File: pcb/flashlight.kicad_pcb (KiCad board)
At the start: 2 copper layers, 16.8 x 15.8 mm, 25 parts, among them IC1 TPS61200, IC2 PIC10F320

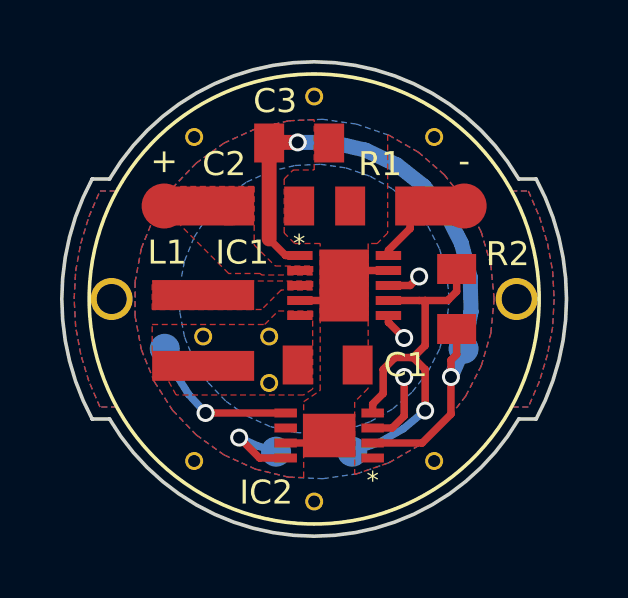
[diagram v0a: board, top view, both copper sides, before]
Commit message: increase width of the vdd and led traces
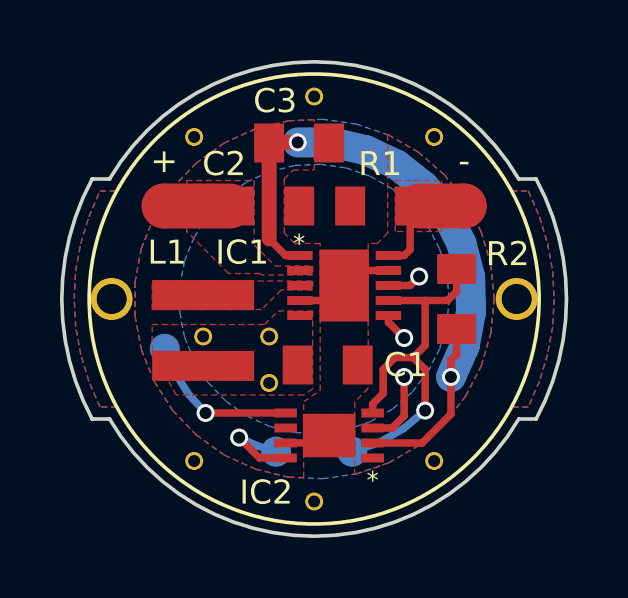
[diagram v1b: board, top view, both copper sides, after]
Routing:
- added copper zone on F.Cu, net N$5
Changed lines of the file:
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@@
   (layers
     (0 F.Cu signal)
-    (31 B.Cu signal)
+    (31 B.Cu signal hide)
     (32 B.Adhes user)
     (33 F.Adhes user)
@@
     (36 B.SilkS user)
     (37 F.SilkS user)
-    (38 B.Mask user)
+    (38 B.Mask user hide)
     (39 F.Mask user)
     (40 Dwgs.User user)
@@
     (last_trace_width 0.25)
     (user_trace_width 0.5)
-    (user_trace_width 1.3)
+    (user_trace_width 1)
+    (user_trace_width 1.5)
     (trace_clearance 0.2)
     (zone_clearance 0.1)
@@
   (segment (start 149.45 94.78) (end 148.52 94.78) (width 0.5) (layer F.Cu) (net 3))
   (via (at 149.45 94.78) (size 0.6) (drill 0.4) (layers F.Cu B.Cu) (net 3))
-  (segment (start 149.45 94.78) (end 150.6 94.78) (width 0.5) (layer B.Cu) (net 3))
-  (segment (start 150.6 94.78) (end 151.72 95.04) (width 0.5) (layer B.Cu) (net 3))
-  (segment (start 151.72 95.04) (end 152.76 95.53) (width 0.5) (layer B.Cu) (net 3))
-  (segment (start 152.76 95.53) (end 153.66 96.24) (width 0.5) (layer B.Cu) (net 3))
-  (segment (start 153.66 96.24) (end 154.39 97.13) (width 0.5) (layer B.Cu) (net 3))
-  (segment (start 154.39 97.13) (end 154.91 98.15) (width 0.5) (layer B.Cu) (net 3))
-  (segment (start 154.91 98.15) (end 155.2 99.27) (width 0.5) (layer B.Cu) (net 3))
-  (segment (start 155.2 99.27) (end 155.23 100.42) (width 0.5) (layer B.Cu) (net 3))
-  (segment (start 155.23 100.42) (end 155.02 101.55) (width 0.5) (layer B.Cu) (net 3))
-  (segment (start 155.02 101.55) (end 154.56 102.6) (width 0.5) (layer B.Cu) (net 3))
+  (segment (start 149.45 94.78) (end 150.6 94.78) (width 1) (layer B.Cu) (net 3))
+  (segment (start 150.6 94.78) (end 151.72 95.04) (width 1) (layer B.Cu) (net 3))
+  (segment (start 151.72 95.04) (end 152.76 95.53) (width 1) (layer B.Cu) (net 3))
+  (segment (start 152.76 95.53) (end 153.66 96.24) (width 1) (layer B.Cu) (net 3))
+  (segment (start 153.66 96.24) (end 154.39 97.13) (width 1) (layer B.Cu) (net 3))
+  (segment (start 154.39 97.13) (end 154.91 98.15) (width 1) (layer B.Cu) (net 3))
+  (segment (start 154.91 98.15) (end 155.2 99.27) (width 1) (layer B.Cu) (net 3))
+  (segment (start 155.2 99.27) (end 155.23 100.42) (width 1) (layer B.Cu) (net 3))
+  (segment (start 155.23 100.42) (end 155.02 101.55) (width 1) (layer B.Cu) (net 3))
+  (segment (start 155.02 101.55) (end 154.56 102.6) (width 1) (layer B.Cu) (net 3))
   (via (at 154.56 102.6) (size 0.6) (drill 0.4) (layers F.Cu B.Cu) (net 3))
-  (segment (start 147.25 96.9) (end 145 96.9) (width 1.3) (layer F.Cu) (net 5))
+  (segment (start 147.2 96.9) (end 145 96.9) (width 1.5) (layer F.Cu) (net 5))
   (segment (start 153.7 101.55) (end 153.7 100.05) (width 0.25) (layer F.Cu) (net 6))
   (segment (start 153.3 101.95) (end 153.7 101.55) (width 0.25) (layer F.Cu) (net 6))
@@
   (segment (start 152.7 101.95) (end 153.2 101.95) (width 0.25) (layer F.Cu) (net 6))
   (segment (start 153.2 101.95) (end 153.25 101.95) (width 0.25) (layer F.Cu) (net 6))
-  (segment (start 152.475 98.55) (end 152.475 98.375) (width 0.25) (layer F.Cu) (net 7))
-  (segment (start 153.2 97.65) (end 153.2 96.9) (width 0.25) (layer F.Cu) (net 7))
-  (segment (start 152.475 98.375) (end 153.2 97.65) (width 0.25) (layer F.Cu) (net 7))
-  (segment (start 153.4 96.9) (end 155 96.9) (width 1.3) (layer F.Cu) (net 7))
+  (segment (start 152.475 98.55) (end 153 98.55) (width 0.25) (layer F.Cu) (net 7) (status 400000))
+  (segment (start 153.2 98.35) (end 153.2 96.9) (width 0.25) (layer F.Cu) (net 7) (status 800000))
+  (segment (start 153 98.55) (end 153.2 98.35) (width 0.25) (layer F.Cu) (net 7))
+  (segment (start 153.5 96.9) (end 155 96.9) (width 1.5) (layer F.Cu) (net 7))
   (segment (start 149.05 103.8) (end 146.38 103.8) (width 0.25) (layer F.Cu) (net 8))
   (via (at 146.38 103.8) (size 0.6) (drill 0.4) (layers F.Cu B.Cu) (net 8))
@@
       (pts
         (xy 148 98.2) (xy 148.7 98.9) (xy 149.95 98.9) (xy 149.95 99.2) (xy 148.25 99.2)
-        (xy 148.2 99.15) (xy 147.15 99.15) (xy 145.55 97.55) (xy 145.55 96.25) (xy 148 96.25)
+        (xy 148.2 99.15) (xy 147.15 99.15) (xy 145.75 97.75) (xy 145.75 96.05) (xy 148 96.05)
       )
     )
@@
       )
     )
+  )
+  (zone (net 7) (net_name N$5) (layer F.Cu) (hatch edge 0.508)
+    (connect_pads yes (clearance 0.1))
+    (min_thickness 0.1)
+    (fill (arc_segments 16) (thermal_gap 0.2) (thermal_bridge_width 0.2))
+    (polygon
+      (pts
+        (xy 154.25 97.75) (xy 152.7 97.75) (xy 152.7 96.05) (xy 154.25 96.05)
+      )
+    )
